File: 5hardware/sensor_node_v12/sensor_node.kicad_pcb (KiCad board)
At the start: 2 copper layers, 30.2 x 24 mm, 38 parts, among them J1 Conn_01x08_Socket, J2 Conn_01x08_Socket, Q2 AO3401A, Q3 MMBT5551L, Q4 AO3401A, SW2 SW_Push, SW4 SW_Reed, SW5 SW_Push, SW6 SW_Push, U1 ESP-12F, U12 APDS-9960, U13 SHT31-DIS, U17 BH1750FVI-TR, U2 2N7002DW, U4 CH32V003F4P6, U7 XC6206PxxxMR, U8 TPL5110

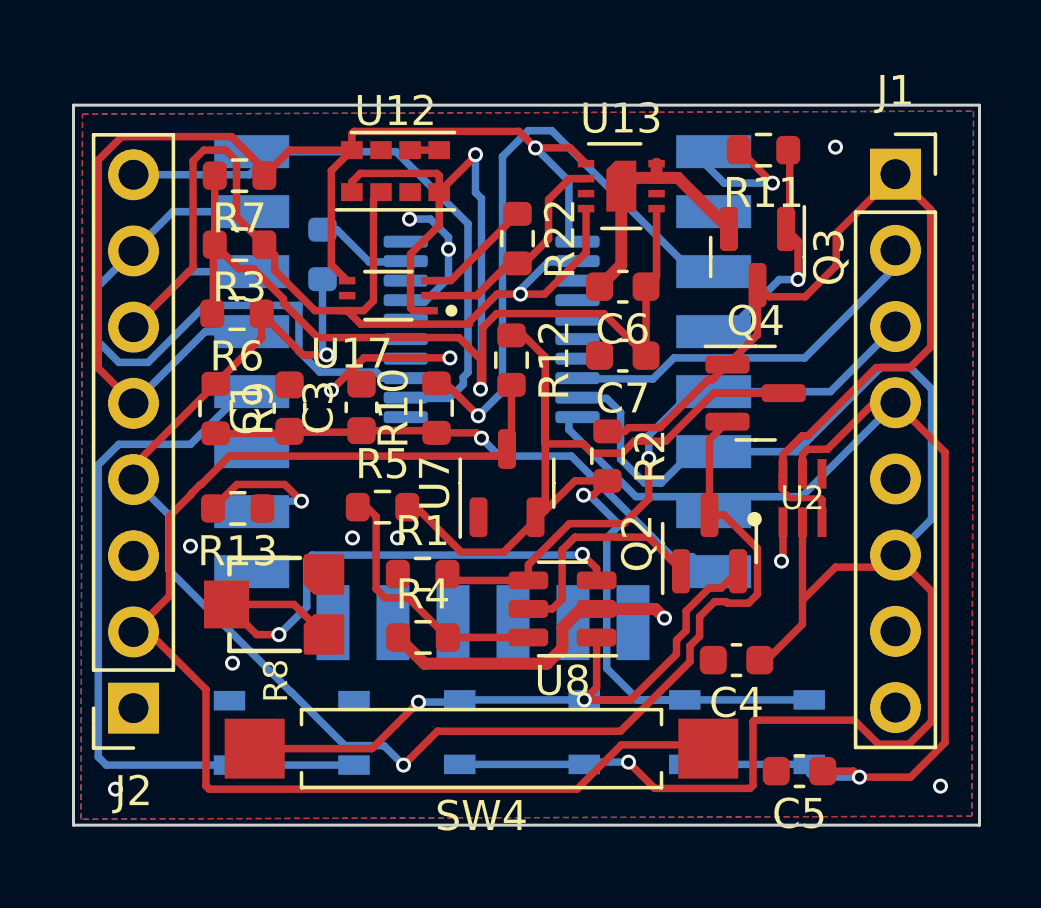
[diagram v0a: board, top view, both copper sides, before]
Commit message: added INA219 and INA226 test.
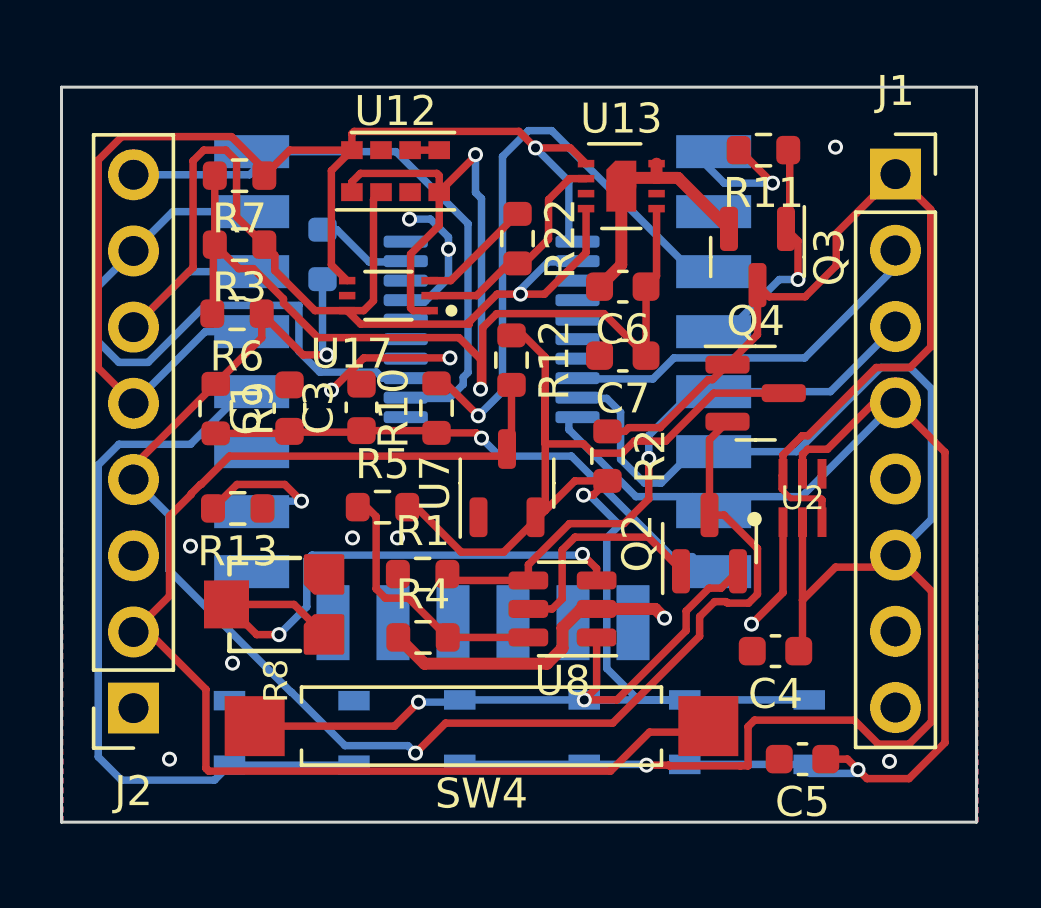
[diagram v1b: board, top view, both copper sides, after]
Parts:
- moved C4 1.33 mm to (176.5, 62.2)
- moved SW4 0.75 mm to (166.7, 64.7)
- moved C5 0.41 mm to (177.4, 65.8)
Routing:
- net GND: track 33.6 -> 36.1 mm
- net SW-B: track 56.8 -> 54.6 mm
- net Net-(Q2-S): track 65.2 -> 64.5 mm
- net +3.3V: track 49.0 -> 48.3 mm
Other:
- board size 30.2 x 24 mm -> 30.5 x 24.5 mm

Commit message: did some works.
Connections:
- J2 pad 3: unconnected-(J2-Pin_3-Pad3) -> +3.3V
- J2 pad 4: +3.3V -> D15
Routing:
- net D15: track 4.62 -> 10.2 mm
